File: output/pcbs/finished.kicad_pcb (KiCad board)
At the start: 4 copper layers, 121 x 101.5 mm, 62 parts

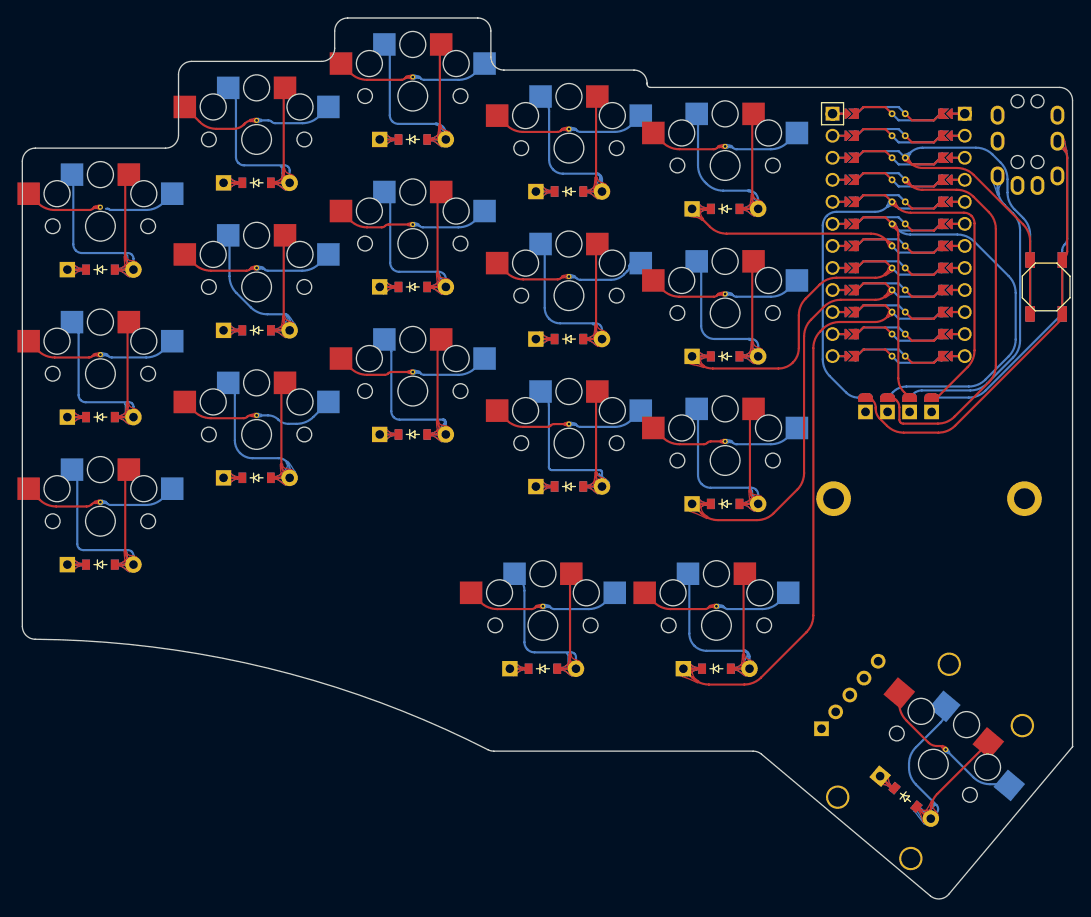
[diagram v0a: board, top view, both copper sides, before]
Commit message: finished PCB, all DRC errors accounted for
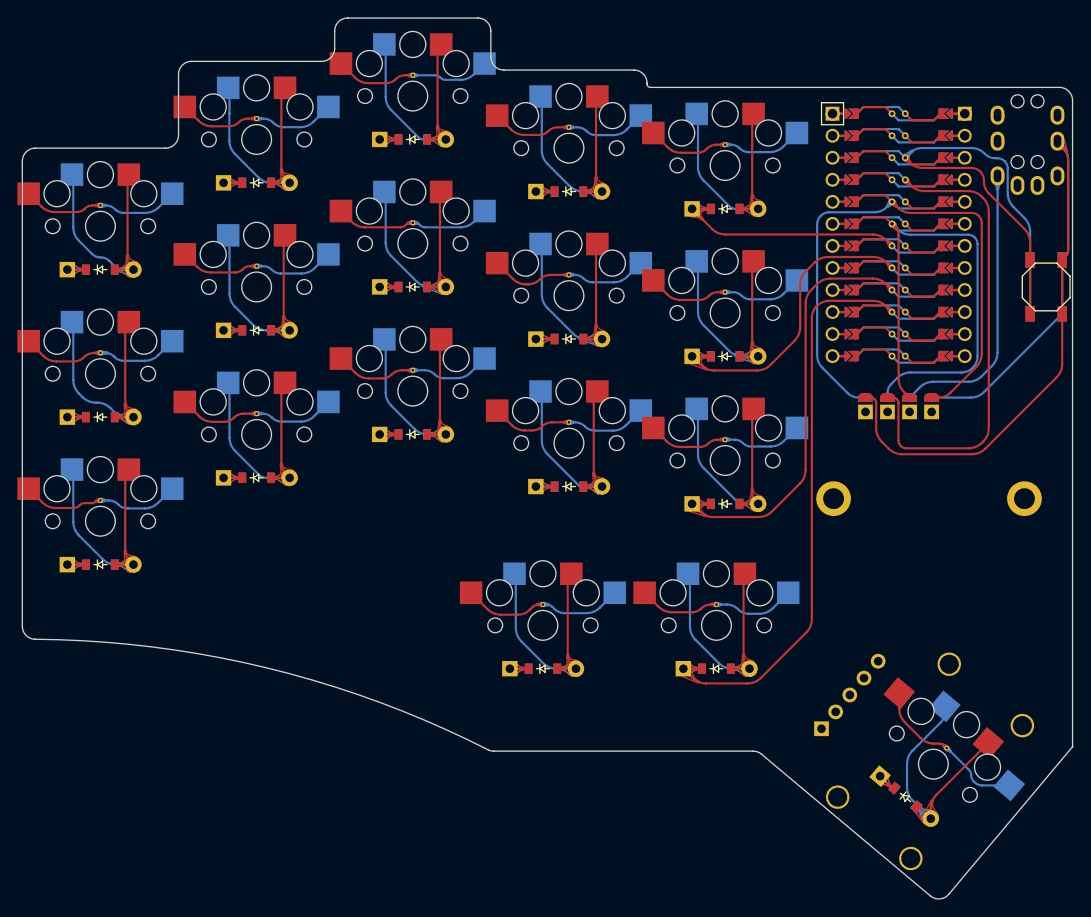
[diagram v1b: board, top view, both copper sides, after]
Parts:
- removed the REF** at (36.0, -17.2)
- removed the REF** at (0.00, -19.2)
- removed the REF** at (18.0, -46.2)
- removed the REF** at (72.0, -9.20)
- removed the REF** at (18.0, -12.2)
- removed the REF** at (18.0, -29.2)
- removed the REF** at (72.0, -43.2)
- removed the REF** at (0.00, -36.2)
- removed the REF** at (36.0, -51.2)
- removed the REF** at (54.0, -45.2)
- removed the REF** at (36.0, -34.2)
- removed the REF** at (51.0, 9.80)
- removed the REF** at (97.4, 26.3)
- removed the REF** at (72.0, -26.2)
- removed the REF** at (0.00, -2.20)
- removed the REF** at (54.0, -11.2)
- removed the REF** at (71.0, 9.80)
- removed the REF** at (54.0, -28.2)
- added REF**: VIA-0.6mm, VIA-0.6mm, F.Cu at (18.0, -46.4)
- added REF**: VIA-0.6mm, VIA-0.6mm, F.Cu at (36.0, -17.4)
- added REF**: VIA-0.6mm, VIA-0.6mm, F.Cu at (71.0, 9.60)
- added REF**: VIA-0.6mm, VIA-0.6mm, F.Cu at (97.5, 26.2)
- added REF**: VIA-0.6mm, VIA-0.6mm, F.Cu at (36.0, -51.4)
- added REF**: VIA-0.6mm, VIA-0.6mm, F.Cu at (72.0, -9.40)
- added REF**: VIA-0.6mm, VIA-0.6mm, F.Cu at (0.00, -19.4)
- added REF**: VIA-0.6mm, VIA-0.6mm, F.Cu at (18.0, -12.4)
- added REF**: VIA-0.6mm, VIA-0.6mm, F.Cu at (51.0, 9.60)
- added REF**: VIA-0.6mm, VIA-0.6mm, F.Cu at (54.0, -11.4)
- added REF**: VIA-0.6mm, VIA-0.6mm, F.Cu at (18.0, -29.4)
- added REF**: VIA-0.6mm, VIA-0.6mm, F.Cu at (54.0, -28.4)
- added REF**: VIA-0.6mm, VIA-0.6mm, F.Cu at (0.00, -36.4)
- added REF**: VIA-0.6mm, VIA-0.6mm, F.Cu at (54.0, -45.4)
- added REF**: VIA-0.6mm, VIA-0.6mm, F.Cu at (0.00, -2.40)
- added REF**: VIA-0.6mm, VIA-0.6mm, F.Cu at (72.0, -43.4)
- added REF**: VIA-0.6mm, VIA-0.6mm, F.Cu at (72.0, -26.4)
- added REF**: VIA-0.6mm, VIA-0.6mm, F.Cu at (36.0, -34.4)
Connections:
- _20 pad : VCC -> P2
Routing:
- net P15: track 200.1 -> 193.1 mm
- net GND: track 178.1 -> 184.7 mm
- net P20: track 193.2 -> 199.0 mm
- net P2: track 143.7 -> 149.1 mm
- net P7: track 122.4 -> 126.7 mm
- net VCC: track 175.9 -> 180.1 mm
- net far_bottom: track 31.9 -> 27.9 mm
- net P6: track 151.7 -> 154.9 mm
- net middle_top: track 31.4 -> 28.3 mm
- net far_top: track 31.2 -> 28.4 mm
- net ring_bottom: track 31.1 -> 28.4 mm
- net P5: track 139.4 -> 142.0 mm
- net P18: track 203.4 -> 205.7 mm
- net P14: track 186.0 -> 188.1 mm
- net index_bottom: track 32.1 -> 30.3 mm
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
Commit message: 2 layer edition featuring gerber files
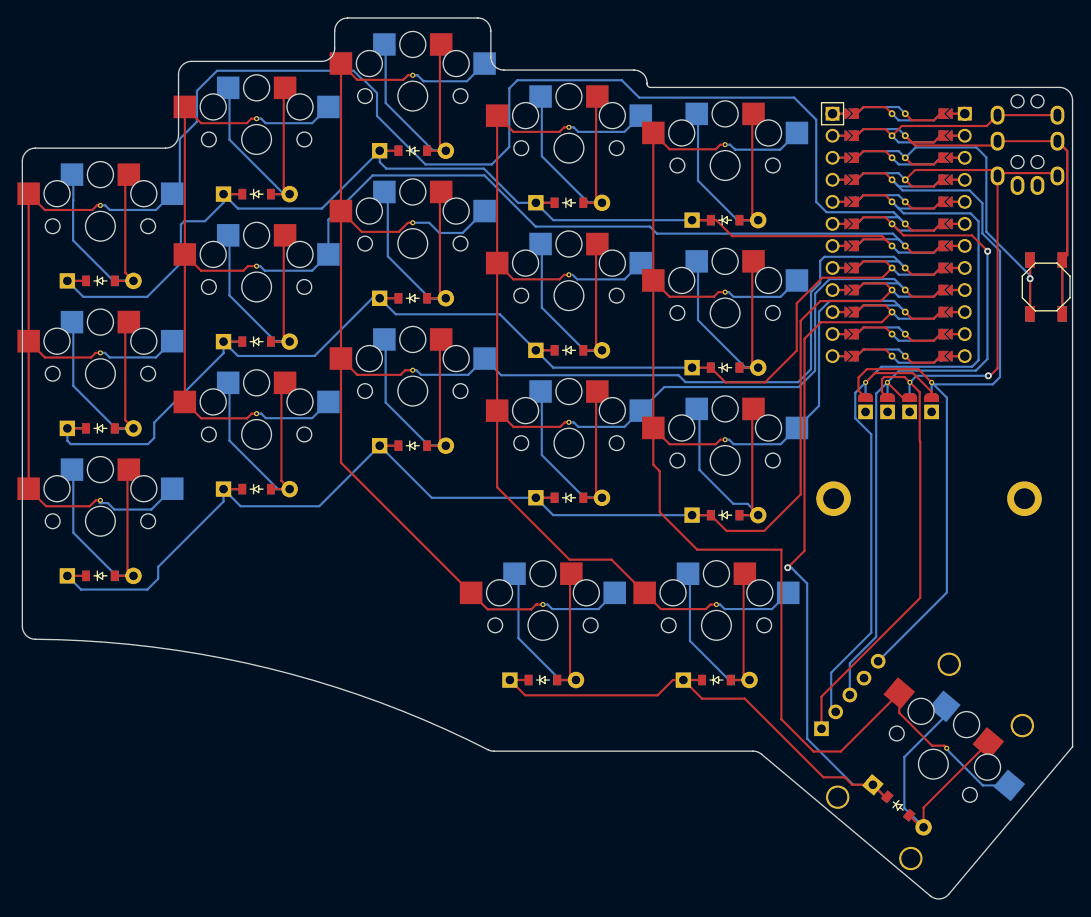
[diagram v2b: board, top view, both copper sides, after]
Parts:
- removed _19: , ProMicro
- removed _20: , pimoroni_trackball
- removed _21: OLED-double-sided, OLED-128x32-double-sided
- added REF**: VIA-0.6mm, VIA-0.6mm, F.Cu at (95.8, -16.0)
- added REF**: VIA-0.6mm, VIA-0.6mm, F.Cu at (93.3, -16.0)
- added REF**: VIA-0.6mm, VIA-0.6mm, F.Cu at (90.7, -16.0)
- added REF**: VIA-0.6mm, VIA-0.6mm, F.Cu at (88.2, -16.0)
- added _23: , ProMicro, F.Cu at (92.0, -33.0)
- added _24: , pimoroni_trackball, F.Cu at (93.7, 26.1)
- added _25: OLED-double-sided, OLED-128x32-double-sided, F.Cu at (86.0, -11.0)
- moved D18 1.30 mm to (92.0, 32.8)
- moved D11 1.30 mm to (54.0, -19.7)
- moved D14 1.30 mm to (72.0, -17.7)
- moved D16 1.30 mm to (51.0, 18.3)
- moved D17 1.30 mm to (71.0, 18.3)
- moved D2 1.30 mm to (0.00, -10.7)
- moved D3 1.30 mm to (0.00, -27.7)
- moved D5 1.30 mm to (18.0, -20.7)
- moved D7 1.30 mm to (36.0, -8.70)
- moved D8 1.30 mm to (36.0, -25.7)
- moved D13 1.30 mm to (72.0, -0.70)
- moved D1 1.30 mm to (0.00, 6.30)
- moved D10 1.30 mm to (54.0, -2.70)
- moved D4 1.30 mm to (18.0, -3.70)
- moved D12 1.30 mm to (54.0, -36.7)
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- renumbered Mount1 to Mount2
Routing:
- net VCC: track 180.1 -> 104.4 mm, vias 0 -> 1
- net P2: track 149.1 -> 93.7 mm
- net P3: track 132.7 -> 80.3 mm, vias 0 -> 1
- net GND: track 184.7 -> 150.1 mm
- net RST: track 58.4 -> 38.8 mm, vias 0 -> 1
- net P20: track 199.0 -> 212.2 mm
- net P15: track 193.1 -> 181.1 mm
- net P14: track 188.1 -> 196.9 mm
- net P19: track 174.2 -> 165.6 mm
- net far_bottom: track 27.9 -> 33.1 mm
- net far_top: track 28.4 -> 33.5 mm
- net ring_bottom: track 28.4 -> 33.1 mm
- net middle_top: track 28.3 -> 32.9 mm
- net P7: track 126.7 -> 130.6 mm, vias 0 -> 1
- net pinky_top: track 30.4 -> 33.7 mm
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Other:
- copper layers 4 -> 2
